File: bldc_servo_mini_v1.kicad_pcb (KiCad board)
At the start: 4 copper layers, 28 x 28 mm, 57 parts, among them IC1 DRV8313PWP, J1 Conn_01x05_MountingPin, J3 Conn_01x03, J6 Conn_01x05_MountingPin, U3 SN65HVD234, U5 STM32G431CBUx

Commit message: wip
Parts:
- removed FPC_SENSOR2: FPC-8PIN, HCTL HC-FPC-05-09-8RLTAG:FPC-SMD_8P-P0.50_HC-FPC-05-09-8RLTAG
- removed U4: ~, SC60228:SOIC-8_L5.0-W4.0-P1.27-LS6.0-BL
- added U2: MT6701QT, Package_DFN_QFN:QFN-16-1EP_3x3mm_P0.5mm_EP1.7x1.7mm, F.Cu at (100.0, 100.0)
- U1: value ~ -> MT6701QT; footprint SC60228:SOIC-8_L5.0-W4.0-P1.27-LS6.0-BL -> Package_DFN_QFN:QFN-16-1EP_3x3mm_P0.5mm_EP1.7x1.7mm
- moved U1 128.5 mm to (47.0, -17.1), turned to 0 degrees
- moved C11 37.6 mm to (46.0, -8.11), turned to 0 degrees
- moved H5 27.1 mm to (41.4, -16.7)
- moved H6 27.1 mm to (41.4, -10.8)
- moved C7 7.28 mm to (97.3, 100.0), turned to -90 degrees
- moved C13 0.60 mm to (103.0, 100.4), turned to 90 degrees
- moved C1 0.20 mm to (105.0, 110.2)
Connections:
- FPC_BOARD1 pad 6: /CS -> /CS_EXTERNAL
- U1 pad 1: /CS -> unconnected-(U1-NC-Pad1)
- U1 pad 3: +3.3V -> unconnected-(U1-NC-Pad3)
- U1 pad 4: GND -> unconnected-(U1-NC-Pad4)
- U1 pad 6: /MISO -> /SENSOR2_MISO
- U1 pad 7: /MOSI -> /SENSOR2_SCK
- U1 pad 8: /SCK -> /SENSOR2_CS
- U5 pad 12: /CAN_EN -> /CS_EXTERNAL
- U5 pad 47: unconnected-(U5-PB9-Pad47) -> /CAN_EN
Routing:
- net /SENSOR2_GND: track 28.8 -> 0.00 mm, vias 3 -> 0
- net /MOSI: track 36.8 -> 12.2 mm
- net /SENSOR2_MISO: track 15.5 -> 0.00 mm
- net /CS_EXTERNAL: track 0.00 -> 14.3 mm, vias 0 -> 2
- net /CAN_EN: track 1.48 -> 15.8 mm, vias 1 -> 2
- net /SENSOR2_SCK: track 12.0 -> 0.00 mm
- net /SENSOR2_MOSI: track 11.8 -> 0.00 mm, vias 2 -> 0
- net /SENSOR2_3V3: track 11.0 -> 0.00 mm
- net /MISO: track 30.6 -> 22.3 mm
- net /SENSOR2_CS: track 5.92 -> 0.00 mm
- net GND: track 29.6 -> 35.3 mm, vias 114 -> 116
- net /CS: track 12.5 -> 10.6 mm, vias 2 -> 1
- net /SWO: track 11.8 -> 10.2 mm
- net +3.3V: track 40.5 -> 41.7 mm, vias 11 -> 10
- net /SCK: track 20.5 -> 19.8 mm

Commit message: 6 layer board draft
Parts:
- removed C11, C14, C15, C30, C32: 100n, Capacitor_SMD:C_0402_1005Metric_Pad0.74x0.62mm_HandSolder
- removed C12, C8: 10u, Capacitor_SMD:C_0805_2012Metric_Pad1.18x1.45mm_HandSolder
- removed H2, H5, H6: MountingHole_Pad, MountingHole:MountingHole_2.2mm_M2_Pad_TopBottom
- removed IC1: DRV8313PWP, DRV8313PWP:SOP65P640X120-29N
- removed J3: Conn_01x03, Connector_JST:JST_PH_S3B-PH-SM4-TB_1x03-1MP_P2.00mm_Horizontal
- removed J5: ~, positive_altitude:Positive_Altitude_SWD_Connector_V2
- removed NT1, NT2, NT3: NetTie_2, positive_altitude:NetTie-2_SMD_Pad0.2mm
- removed R13, R16, R29: 10m, 0.1W+, 0603, Resistor_SMD:R_0603_1608Metric_Pad0.98x0.95mm_HandSolder
- removed R19, R21, R25: 67k, Resistor_SMD:R_0402_1005Metric_Pad0.72x0.64mm_HandSolder
- removed R20, R22, R23, R24, R26, R27: 2.2k, Resistor_SMD:R_0402_1005Metric_Pad0.72x0.64mm_HandSolder
- removed U1: MT6701QT, Package_DFN_QFN:QFN-16-1EP_3x3mm_P0.5mm_EP1.7x1.7mm
- removed U5: STM32G431CBUx, Package_DFN_QFN:QFN-48-1EP_7x7mm_P0.5mm_EP5.6x5.6mm
- added C17: 100n, Capacitor_SMD:C_0402_1005Metric_Pad0.74x0.62mm_HandSolder, B.Cu at (101.6, 107.5)
- added C18: 22u, Capacitor_SMD:C_1210_3225Metric_Pad1.33x2.70mm_HandSolder, B.Cu at (102.4, 109.6)
- added C19: 100u, Capacitor_SMD:CP_Elec_6.3x5.8, B.Cu at (96.3, 107.6)
- added C20: 100n, Capacitor_SMD:C_0402_1005Metric_Pad0.74x0.62mm_HandSolder, B.Cu at (106.1, 106.4)
- added IC2: DRV8311HRRWR, DRV8311HRRWR:DRV8311PRRWR, B.Cu at (104.5, 103.6)
- added J2: Positive_Altitude_SWD_Connector, positive_altitude:Positive_Altitude_SWD_Connector, F.Cu at (90.0, 100.0)
- added J4: Conn_01x03_MountingPin, Connector_JST:JST_PH_S3B-PH-SM4-TB_1x03-1MP_P2.00mm_Horizontal, B.Cu at (98.0, 95.5)
- added JP2: SolderJumper_2_Open, Jumper:SolderJumper-2_P1.3mm_Open_RoundedPad1.0x1.5mm, B.Cu at (109.2, 107.2)
- added R1: 47k, Resistor_SMD:R_0402_1005Metric_Pad0.72x0.64mm_HandSolder, B.Cu at (108.0, 104.4)
- added U4: STM32G431KBUx, Package_DFN_QFN:QFN-32-1EP_5x5mm_P0.5mm_EP3.45x3.45mm, F.Cu at (97.3, 92.0)
- C1, C13, C2, C3, C33, C4, C5, FB1: moved to F.Cu
- C16: value 10n -> 4.7u; footprint Capacitor_SMD:C_0402_1005Metric_Pad0.74x0.62mm_HandSolder -> Capacitor_SMD:C_0603_1608Metric_Pad1.08x0.95mm_HandSolder; moved to B.Cu
- C6: moved to B.Cu
- C9: value 470n -> 100n; moved to B.Cu
- D2: value TVS 26V -> TVS 17V
- PAD4: value VIN -> GND
- PAD5: value GND -> VCC
- U3: value SN65HVD234 -> SN65HVD230
- moved C2 24.3 mm to (98.5, 87.4), turned to 0 degrees
- moved R3 23.7 mm to (104.9, 88.8), turned to -90 degrees
- moved JP1 22.8 mm to (107.2, 90.0)
- moved C1 21.9 mm to (102.6, 88.4)
- moved PAD4 21.8 mm to (110.0, 106.5), turned to 25 degrees
- moved PAD5 21.8 mm to (90.0, 106.5), turned to -25 degrees
- moved C6 20.4 mm to (103.4, 106.9), turned to 90 degrees
- moved C16 15.5 mm to (105.3, 99.6), turned to 90 degrees
- moved FPC_BOARD1 14.6 mm to (106.5, 92.6), turned to 180 degrees
- moved C3 13.8 mm to (101.3, 88.1), turned to -90 degrees
- moved U3 13.6 mm to (105.3, 94.2), turned to 0 degrees
- moved C33 13.5 mm to (91.6, 91.4), turned to 0 degrees
- moved C5 13.5 mm to (91.6, 92.4), turned to 0 degrees
- moved D2 12.7 mm to (91.5, 107.1), turned to 90 degrees
- moved C9 10.6 mm to (101.6, 106.4), turned to 180 degrees
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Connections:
- C16 pad 1: Net-(IC1-CPL) -> /DRIVER_AVDD
- C16 pad 2: Net-(IC1-CPH) -> GND
- C6 pad 1: Net-(IC1-VCP) -> VCC
- C6 pad 2: VCC -> /DRIVER_CP
- C9 pad 1: Net-(IC1-V3P3) -> VCC
- JP1 pad 1: /CAN_H -> /CAN_L
- PAD4 pad 1: VCC -> GND
- PAD5 pad 1: GND -> VCC
- R3 pad 2: /CAN_L -> /CAN_H
- U3 pad 5: /CAN_EN -> unconnected-(U3-Vref-Pad5)
- U3 pad 8: /CAN_Rs -> GND
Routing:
- net /PWM_L1: track 0.00 -> 52.7 mm, vias 0 -> 2
- net +3.3V: track 41.7 -> 93.1 mm, vias 10 -> 9
- net /PWM_L2: track 0.00 -> 51.1 mm, vias 0 -> 2
- net /CURRENT2: track 0.00 -> 32.1 mm, vias 0 -> 2
- net /VOLTAGE_SENCE: track 2.57 -> 34.5 mm, vias 0 -> 2
- net /CURRENT1: track 0.00 -> 29.9 mm, vias 0 -> 2
- net /CURRENT3: track 0.00 -> 29.3 mm, vias 0 -> 2
- net /DRIVER_SLEW: track 0.00 -> 27.8 mm, vias 0 -> 2
- net /SHUNT3+: track 26.7 -> 0.00 mm, vias 1 -> 0
- net VDDA: track 8.35 -> 34.7 mm, vias 0 -> 1
- net /SHUNT2+: track 26.0 -> 0.00 mm, vias 1 -> 0
- net /SHUNT3-: track 25.5 -> 0.00 mm, vias 1 -> 0
- net /SHUNT2-: track 24.9 -> 0.00 mm, vias 1 -> 0
- net /DRIVER_GAIN: track 0.00 -> 24.5 mm, vias 0 -> 2
- net /IN1: track 23.8 -> 0.00 mm, vias 1 -> 0
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- added copper zone on In2.Cu, net GND
- added copper zone on In3.Cu, net GND
- added copper zone on In4.Cu, net GND
- removed copper zone on In2.Cu, net +3.3V
- removed copper zone on F.Cu, net VCC
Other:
- copper layers 4 -> 6

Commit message: Almost finished board and pannel
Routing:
- net VCC: track 36.2 -> 11.0 mm, vias 2 -> 10
- net /OUT2: track 8.91 -> 0.00 mm
- net /OUT1: track 10.8 -> 2.90 mm
- net /OUT3: track 6.92 -> 0.00 mm
- net GND: track 52.5 -> 47.9 mm, vias 20 -> 61
- net /CAN_H: track 35.6 -> 33.4 mm
- net /CAN_L: track 36.2 -> 34.2 mm
- net /NRST: track 16.9 -> 15.0 mm
- net /CURRENT3: track 29.3 -> 30.8 mm
- net /DRIVER_GAIN: track 24.5 -> 25.8 mm
- net /PWM_H3: track 17.2 -> 18.4 mm
- net /PWM_H2: track 20.3 -> 21.3 mm
- net /DRIVER_AVDD: track 11.9 -> 11.1 mm
- net VDDA: track 34.7 -> 33.9 mm
- net /PWM_H1: track 23.7 -> 24.5 mm
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- added copper zone on B.Cu, net /OUT1
- added copper zone on B.Cu, net /OUT2
- added copper zone on B.Cu, net /OUT3
- added copper zone on B.Cu, net VCC
- added copper zone on F.Cu, net VCC

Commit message: Component IDs and cleanup
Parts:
- C19: value 100u -> 47u
- C4: value 1u -> 4.7u
- FPC1: renamed from FPC_BOARD1; value FPC-8PIN -> External_sensor
- J1: value Conn_01x05_MountingPin -> Power_and_data1
- J4: value Conn_01x03_MountingPin -> Motor_connector
- J6: value Conn_01x05_MountingPin -> Power_and_data2
- JP1: value SolderJumper_2_Open -> Enable_CAN_termination
- JP2: value SolderJumper_2_Open -> Enable_3.3V_source
- R4: value 22k -> 47k
- R5: value 4.7k -> 5.1k
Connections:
- U4 pad 10: unconnected-(U4-PA5-Pad10) -> /VOLTAGE_SENCE
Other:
- board text added: "+"
- board text added: "+G3LH"
- board text added: "3"
- board text added: "3 2 1"
- board text added: "3.3V SOURCE"
- board text added: "BLDC SERVO"
- board text added: "C"
- board text added: "D"
- board text added: "G"
- board text added: "POSITIVE ALTITUDE"
- board text added: "R"
- board text added: "SENSOR"
- board text added: "T"
- board text added: "V1.0"

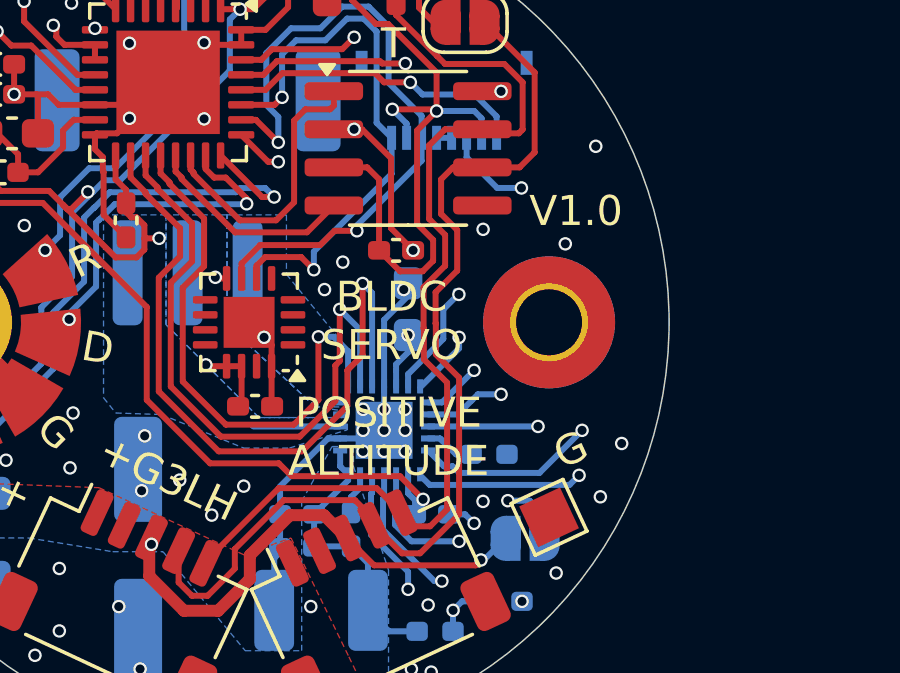
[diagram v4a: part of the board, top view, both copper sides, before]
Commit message: Upgrading to KiCad 9
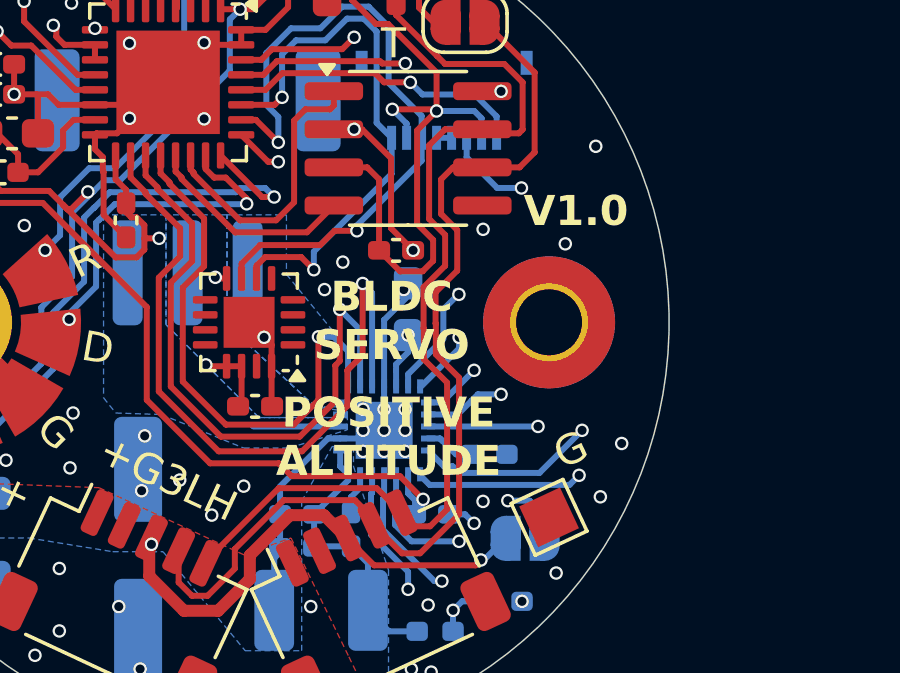
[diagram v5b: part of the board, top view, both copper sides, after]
